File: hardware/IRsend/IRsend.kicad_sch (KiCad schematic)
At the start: 4 parts, among them J1 Conn_01x03_Pin, U1 WEMOS_D1_mini_V4

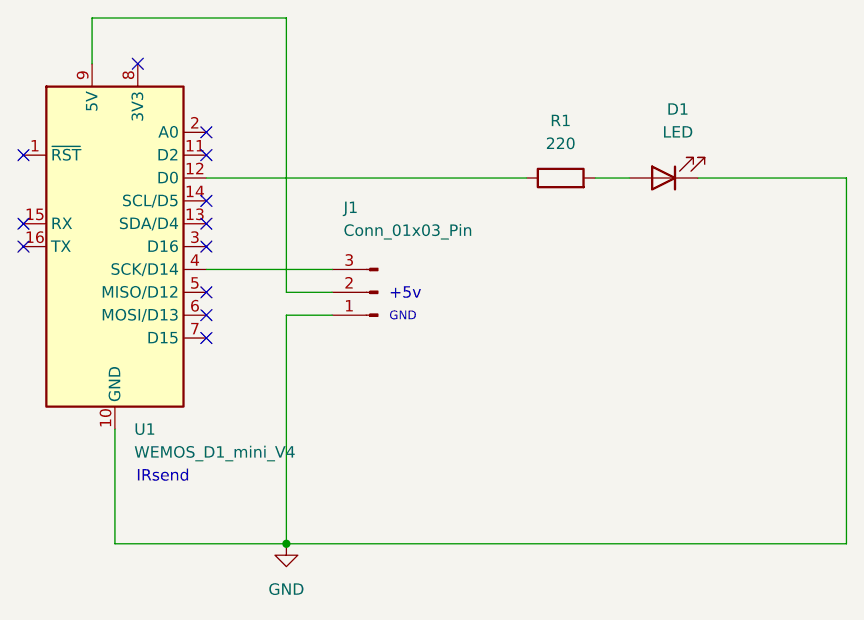
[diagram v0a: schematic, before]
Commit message: Fixed problem with IR signal and GND being swapped on J1.
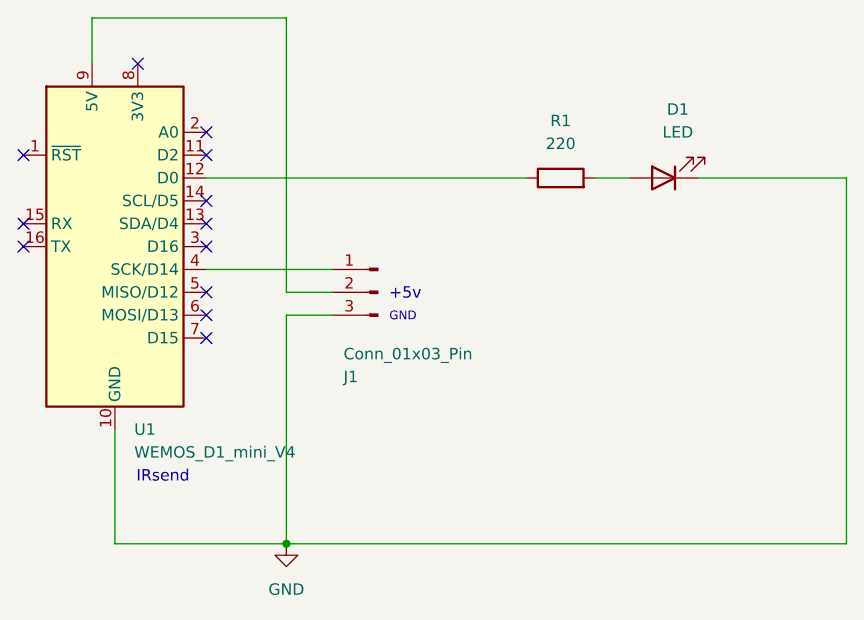
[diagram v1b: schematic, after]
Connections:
- net GND: now also J1.3 (Pin_3); no longer J1.1 (Pin_1)
- net at U1.4 (SCK/D14): now also J1.1 (Pin_1); no longer J1.3 (Pin_3)
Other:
- moved on the sheet: J1
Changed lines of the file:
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@@
+	(wire
+		(pts
+			(xy 59.69 68.58) (xy 64.77 68.58)
+		)
+		(stroke
+			(width 0)
+			(type default)
+		)
+	)
+	(wire
+		(pts
+			(xy 59.69 93.98) (xy 59.69 68.58)
+		)
+		(stroke
+			(width 0)
+			(type default)
+		)
+	)
+	(wire
+		(pts
+			(xy 105.41 53.34) (xy 121.92 53.34)
+		)
+		(stroke
+			(width 0)
+			(type default)
+		)
+	)
+	(wire
+		(pts
+			(xy 38.1 40.64) (xy 38.1 35.56)
+		)
+		(stroke
+			(width 0)
+			(type default)
+		)
+	)
+	(wire
+		(pts
+			(xy 38.1 35.56) (xy 59.69 35.56)
+		)
+		(stroke
+			(width 0)
+			(type default)
+		)
+	)
 	(wire
 		(pts
@@
 	(wire
 		(pts
-			(xy 59.69 93.98) (xy 59.69 68.58)
-		)
-		(stroke
-			(width 0)
-			(type default)
-		)
-	)
-	(wire
-		(pts
-			(xy 105.41 53.34) (xy 121.92 53.34)
-		)
-		(stroke
-			(width 0)
-			(type default)
-		)
-	)
-	(wire
-		(pts
-			(xy 38.1 40.64) (xy 38.1 35.56)
-		)
-		(stroke
-			(width 0)
-			(type default)
-		)
-	)
-	(wire
-		(pts
-			(xy 38.1 35.56) (xy 59.69 35.56)
-		)
-		(stroke
-			(width 0)
-			(type default)
-		)
-	)
-	(wire
-		(pts
 			(xy 40.64 81.28) (xy 40.64 93.98)
 		)
@@
 		(pts
 			(xy 121.92 93.98) (xy 59.69 93.98)
-		)
-		(stroke
-			(width 0)
-			(type default)
-		)
-	)
-	(wire
-		(pts
-			(xy 59.69 68.58) (xy 64.77 68.58)
 		)
 		(stroke
@@
 	(symbol
 		(lib_id "Connector:Conn_01x03_Pin")
-		(at 69.85 66.04 180)
+		(at 69.85 66.04 0)
+		(mirror y)
 		(unit 1)
 		(exclude_from_sim no)
@@
 		(dnp no)
 		(property "Reference" "J1"
-			(at 66.04 56.642 0)
+			(at 66.04 75.438 0)
 			(effects
 				(font
@@
 		)
 		(property "Value" "Conn_01x03_Pin"
-			(at 66.04 59.182 0)
-			(effects
-				(font
+			(at 66.04 72.898 0)
+			(effects
+				(font
